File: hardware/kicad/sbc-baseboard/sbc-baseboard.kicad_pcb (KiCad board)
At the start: 4 copper layers, 140 x 80 mm, 339 parts, among them J1 USB-C upstream, J10 RJ45 magjack 10/100, J11 COM/NO/NC, J12 COM/NO/NC, J13 Console, J14 +5V_TGT out, J15 GPIO + I2C, J16 SWD, J17 Qwiic PD, J18 PSU in (isolated), J19 PSU out (isolated), J2 USB-C PD in, J3 USB-C HID to target, J4 USB-A x2, J5 USB-A x2, J601 SWD (K20), J9 FTDI header, K801 G6K-2F-Y DC5, K802 G6K-2F-Y DC5, K803 JW1FSN-DC5V, Q101 2N7002, Q102 2N7002, Q801 2N7002, Q802 2N7002, Q803 AO3400A, SW201 RESET, SW601 DAP RESET, U101 STUSB4500QTR, U102 PCA9517A, U103 TPS54560BDDA, U104 TPS54560BDDA, U105 TPS62823DLC, U201 MK64FN1M0VLL12, U202 USBLC6-2SC6, U301 KSZ8081RNA, U401 USBLC6-2SC6, U402 USB2517, U403 TPS2553DBV, U404 TPS2553DBV, U405 TPS2553DBV, U406 TPS2553DBV, U407 TPS2553DBV, U408 USBLC6-2SC6, U409 USBLC6-2SC6, U410 USBLC6-2SC6, U411 USBLC6-2SC6, U501 FT231XS, U601 MK20DX128VFM5, U701 TXB0104PW, U702 TXB0108PW, U703 TXS0102DCU, U704 TPS26630RGE, U801 LTV-817, Y201 32.768kHz, Y301 25MHz, Y401 24MHz, Y601 8MHz

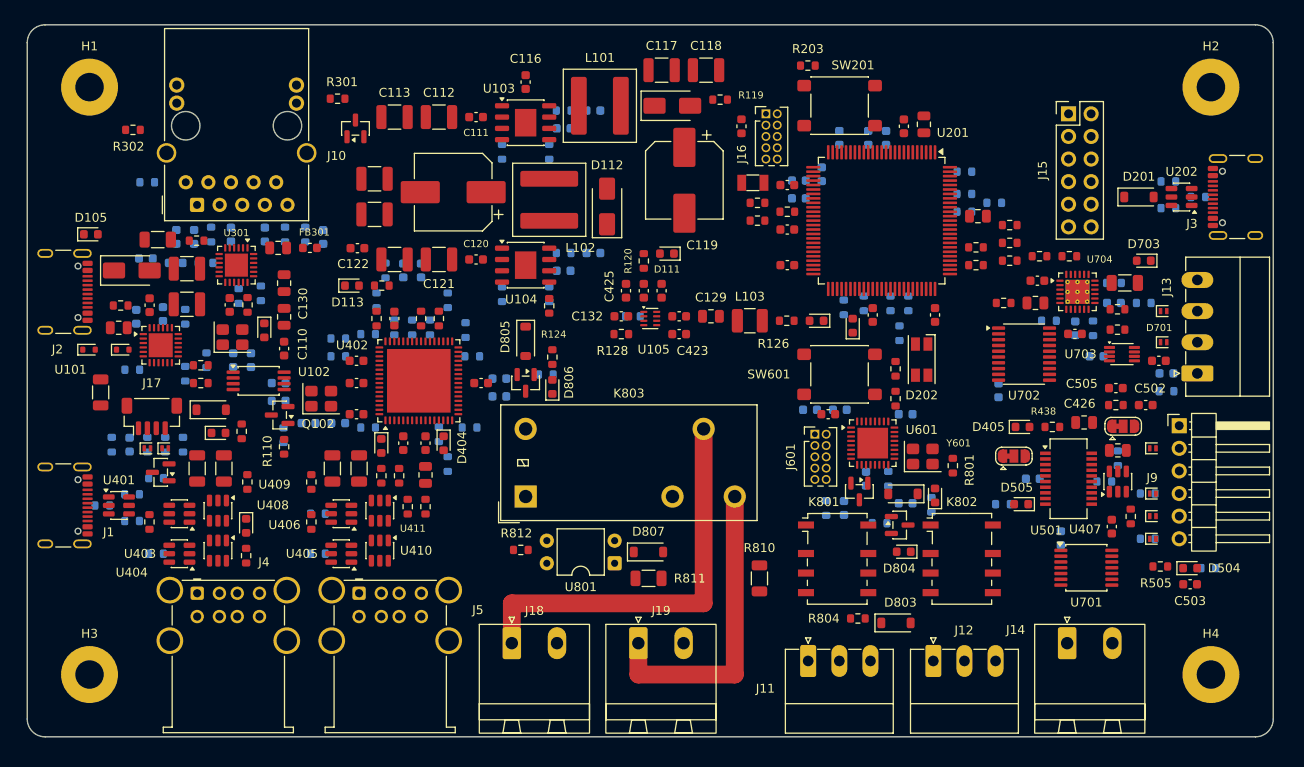
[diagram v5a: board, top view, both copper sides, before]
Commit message: Calibrate the engine against 79 published KiCad boards; the measured practice becomes the standard's numbers
scripts/reference-boards.txt and fetch-reference-boards.sh mirror Olimex,
MNT Reform, SparkFun and Raspberry Pi designs into reference-boards/
(git-ignored); scripts/harvest-placement.py measures each board with
pcbnew (decoupling distance and side, ESD and crystal distance, pad gaps,
edge clearance, bottom-side shares, tuck and through-hole margins,
designator visibility and size, track widths) into docs/reference-boards.csv;
docs/reference-boards.md records the method, the medians and the decisions.

Set from the measurement: decoupling tries its IC's first two rings on top
before the bottom (same side 77 % -> 93 %); ring gap and packing margin
0.15 mm (0.65 mm pad to pad); bottom parts tuck 1.75 mm under the IC and
keep 0.5 mm from through-hole pads; designators 0.8 mm, minimum 0.7 mm with
a 0.1 mm stroke, allowed by the board constraints (visible 61 % -> 75 %).
Kept with reason: the 3 mm edge zone. DRC unchanged, zero warnings; board
reproducible.

Co-Authored-By: Claude Fable 5.1 <noreply@anthropic.com>
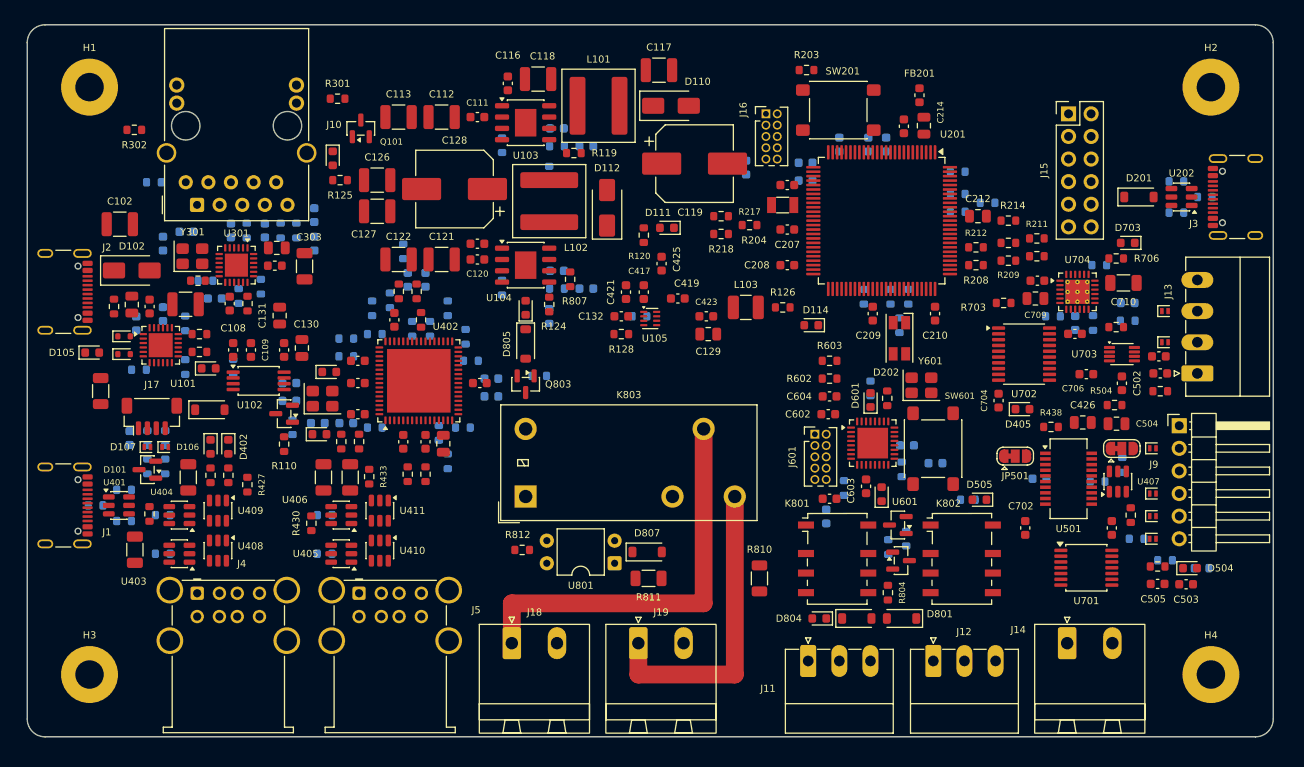
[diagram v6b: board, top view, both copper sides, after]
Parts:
- C108, C109, C602, C603, C604, C701, C702, C704, C706, R701: moved to F.Cu
- moved C505 22.5 mm to (127.0, 62.8)
- moved FB201 20.3 mm to (100.2, 7.91)
- moved C118 18.9 mm to (57.4, 6.09), turned to 180 degrees
- moved R119 17.5 mm to (61.4, 14.4)
- moved C303 16.8 mm to (31.2, 27.1), turned to -90 degrees
- moved D113 14.5 mm to (34.3, 15.0), turned to -90 degrees
- moved D801 14.0 mm to (98.2, 66.7)
- moved D404 14.0 mm to (32.8, 46.0), turned to 0 degrees
- moved C420 13.5 mm to (12.1, 59.0)
- moved C304 13.5 mm to (32.2, 24.6)
- moved C125 13.5 mm to (50.6, 24.6)
- moved SW601 13.4 mm to (101.8, 47.6), turned to 90 degrees
- moved D105 13.3 mm to (7.30, 36.8)
- moved R125 12.7 mm to (35.1, 17.4)
- moved D804 12.1 mm to (89.0, 66.7)
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
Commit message: Pairs laid as lanes, the rails as L3 regions, the Ethernet pairs named: the board ready for the bulk router
All sixteen USB 2.0 pair segments and the two Ethernet MDI pairs are laid
by the standard's placer from pair lanes in gen/layout.py: members at the
class geometry, escapes at the pads, the USB-C receptacles' doubled pads
bridged behind their rows, two pairs passing under the port pairs on the
bottom, every pair matched to within 0.25 mm, no crossings (the port
arrays and the J3 array use the house symbol drawn with I/O2 on top, the
K64's USB pins wired to its rows). J4 and J5 trade places so each stack's
pairs reach the hub row they are wired to. The ESD arrays, the series
parts and the SWD header are anchored for the lanes. The rails are
regions on In2.Cu at distinct priorities over a 3V3 base. The Ethernet
MDI pairs are named ETH_TD/RD and classed ETH (100 ohm). DRC: the 12
documented errors, no warnings but the unfilled rail islands; 499
connections for the bulk router (gen/pcb.py --route), which is running.

Co-Authored-By: Claude Fable 5.1 <noreply@anthropic.com>
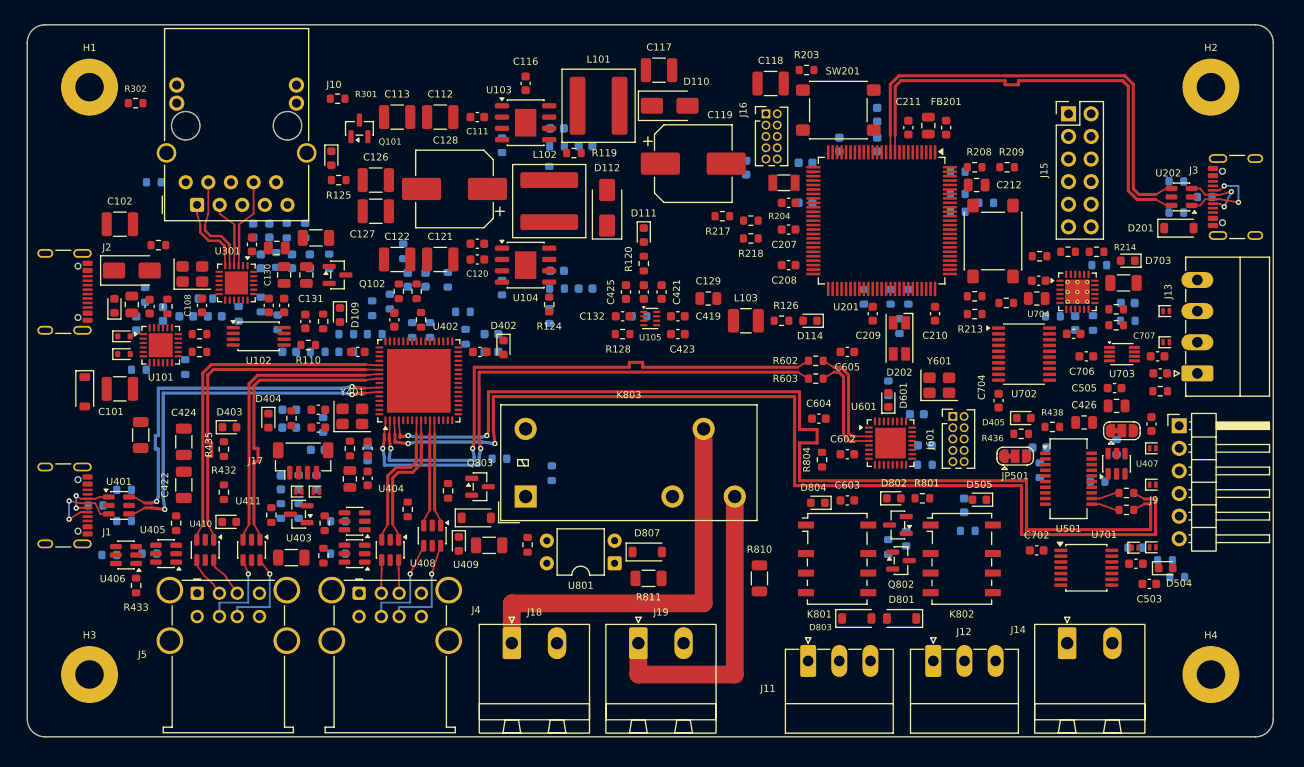
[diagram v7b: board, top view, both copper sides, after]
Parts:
- moved C420 39.8 mm to (51.9, 58.5), turned to 0 degrees
- moved R807 35.0 mm to (29.7, 44.2), turned to 90 degrees
- moved D402 32.9 mm to (53.5, 36.3)
- moved R433 28.9 mm to (12.2, 63.0), turned to 90 degrees
- moved D806 27.6 mm to (48.5, 58.3), turned to -90 degrees
- moved C118 26.1 mm to (83.5, 6.59), turned to 0 degrees
- moved R429 24.8 mm to (47.3, 52.4)
- moved R434 24.6 mm to (9.22, 59.6)
- moved U406 24.6 mm to (11.1, 59.6)
- moved SW601 24.3 mm to (108.5, 24.3)
- moved U409 24.2 mm to (45.5, 57.4)
- moved C505 22.5 mm to (122.2, 40.8)
- moved R604 22.1 mm to (113.8, 50.0)
- moved D805 20.3 mm to (50.5, 55.4), turned to 0 degrees
- moved R424 19.7 mm to (33.4, 56.0)
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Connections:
- net Net-(J10-RD+) renamed /Ethernet/ETH_RD_P
- net Net-(J10-RD-) renamed /Ethernet/ETH_RD_N
- net Net-(J10-TD+) renamed /Ethernet/ETH_TD_P
- net Net-(J10-TD-) renamed /Ethernet/ETH_TD_N
- U202 pad 1: /MCU/J3_D_N -> /MCU/J3_D_P
- U202 pad 3: /MCU/J3_D_P -> /MCU/J3_D_N
- U202 pad 4: /MCU/K64_USB_P -> /MCU/K64_USB_N
- U202 pad 6: /MCU/K64_USB_N -> /MCU/K64_USB_P
- U408 pad 1: /USB hub/HUB_DN4_N -> /USB hub/HUB_DN4_P
- U408 pad 3: /USB hub/HUB_DN4_P -> /USB hub/HUB_DN4_N
- U408 pad 4: /USB hub/PORT1_D_P -> /USB hub/PORT1_D_N
- U408 pad 6: /USB hub/PORT1_D_N -> /USB hub/PORT1_D_P
- U409 pad 1: /USB hub/HUB_DN5_N -> /USB hub/HUB_DN5_P
- U409 pad 3: /USB hub/HUB_DN5_P -> /USB hub/HUB_DN5_N
- U409 pad 4: /USB hub/PORT2_D_P -> /USB hub/PORT2_D_N
- U409 pad 6: /USB hub/PORT2_D_N -> /USB hub/PORT2_D_P
- U410 pad 1: /USB hub/HUB_DN6_N -> /USB hub/HUB_DN6_P
- U410 pad 3: /USB hub/HUB_DN6_P -> /USB hub/HUB_DN6_N
- U410 pad 4: /USB hub/PORT3_D_P -> /USB hub/PORT3_D_N
- U410 pad 6: /USB hub/PORT3_D_N -> /USB hub/PORT3_D_P
- U411 pad 1: /USB hub/HUB_DN7_N -> /USB hub/HUB_DN7_P
- U411 pad 3: /USB hub/HUB_DN7_P -> /USB hub/HUB_DN7_N
- U411 pad 4: /USB hub/PORT4_D_P -> /USB hub/PORT4_D_N
- U411 pad 6: /USB hub/PORT4_D_N -> /USB hub/PORT4_D_P
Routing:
- net HUB_DN2_P: track 0.00 -> 115.2 mm, vias 0 -> 2
- net HUB_DN2_N: track 0.00 -> 115.2 mm, vias 0 -> 2
- net HUB_DN1_N: track 0.00 -> 63.1 mm, vias 0 -> 2
- net HUB_DN1_P: track 0.00 -> 63.1 mm, vias 0 -> 2
- net /MCU/K64_USB_N: track 0.00 -> 50.9 mm
- net /MCU/K64_USB_P: track 0.00 -> 50.9 mm
- net /USB hub/HUB_UP_P: track 0.00 -> 40.7 mm, vias 0 -> 2
- net /USB hub/HUB_UP_N: track 0.00 -> 40.7 mm, vias 0 -> 2
- net /USB hub/HUB_DN6_N: track 0.00 -> 38.2 mm
- net /USB hub/HUB_DN6_P: track 0.00 -> 38.2 mm
- net /USB hub/HUB_DN7_P: track 0.00 -> 31.9 mm
- net /USB hub/HUB_DN7_N: track 0.00 -> 31.8 mm
- net /USB hub/HUB_DN4_N: track 0.00 -> 15.0 mm
- net /USB hub/HUB_DN4_P: track 0.00 -> 15.0 mm
- net /DAPLink/K20_USB_P: track 0.00 -> 12.0 mm
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- added copper zone on In2.Cu, net +3V3
- added copper zone on In2.Cu, net +5V_PORTS
- added copper zone on In2.Cu, net +5V_TGT
- added copper zone on In2.Cu, net VBUS_IN

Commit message: The board routed: the engine's lanes and pairs, then FreeRouting over them; 189 connections left for the hand pass
The autorouter ran over the locked lanes, the pair tracks and the L3
rail regions (gen/pcb.py --route: the corridors open to it, the isolation
region hardened and grown by the creepage, widths capped at 1 mm since
the planes carry the current, inner layers as planes). Twelve passes:
3067 track segments, 297 vias, 189 of 499 connections left, among them the
rail pieces still wanting vias; DRC at the 12 documented USB-C errors with
20 isolated-copper warnings for those pieces. The standards submodule is
at the tool fixes. From here the board file is the source of truth: the
hand pass finishes the connections, stitches the ground at four vias per
square centimetre and floods the outer layers.

Co-Authored-By: Claude Fable 5.1 <noreply@anthropic.com>
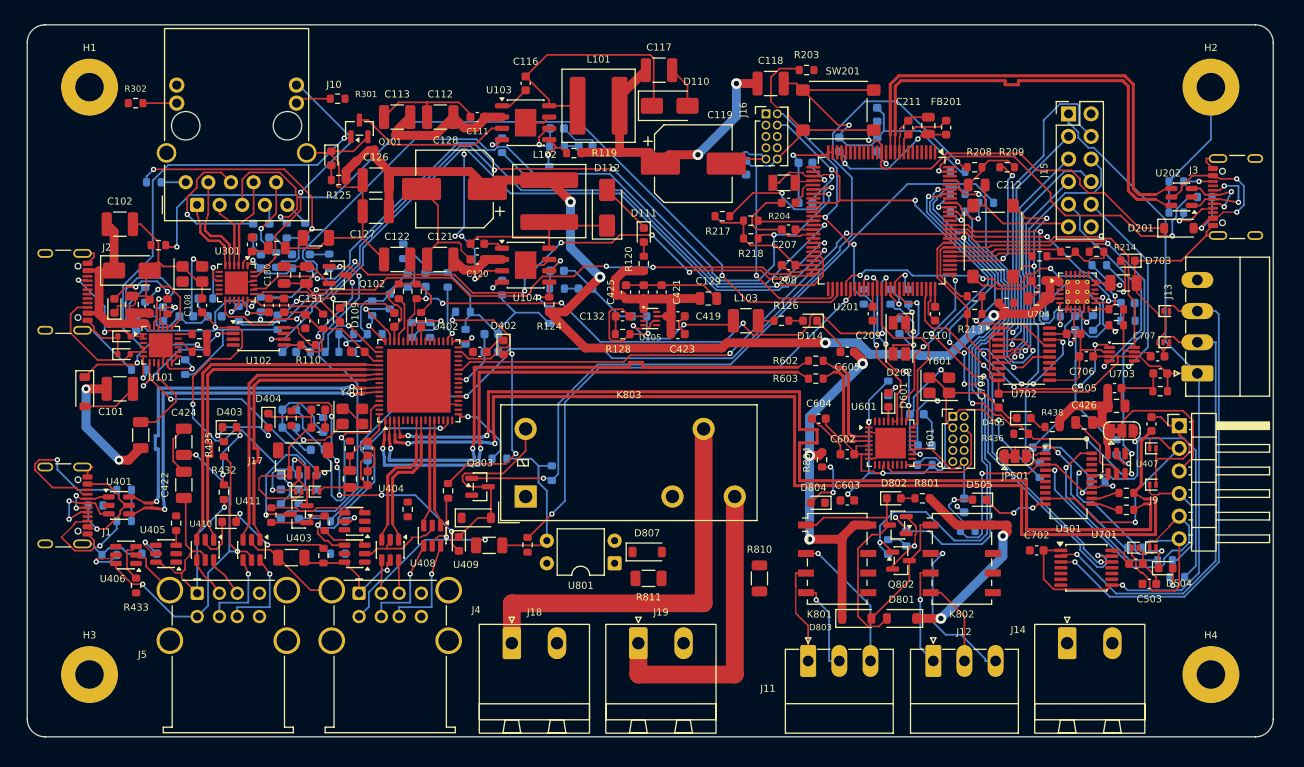
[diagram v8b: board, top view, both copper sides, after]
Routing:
- net GND: track 0.00 -> 702.0 mm, vias 0 -> 6
- net +3V3: track 0.00 -> 129.8 mm
- net +5V_PORTS: track 0.00 -> 126.8 mm, vias 0 -> 7
- net +5V_TGT: track 0.00 -> 122.0 mm, vias 0 -> 4
- net VREF_TGT: track 0.00 -> 120.7 mm, vias 0 -> 1
- net PORT1_FAULT_N: track 0.00 -> 118.1 mm, vias 0 -> 3
- net FTDI_FAULT_N: track 0.00 -> 110.7 mm, vias 0 -> 5
- net MDIO: track 0.00 -> 94.3 mm, vias 0 -> 2
- net I2C0_SDA: track 0.00 -> 91.2 mm, vias 0 -> 5
- net RMII_RXER: track 0.00 -> 88.8 mm, vias 0 -> 2
- net +3V3_PD: track 0.00 -> 87.9 mm, vias 0 -> 4
- net RMII_TXEN: track 0.00 -> 82.6 mm, vias 0 -> 2
- net RMII_RXD0: track 0.00 -> 82.5 mm, vias 0 -> 8
- net RMII_TXD0: track 0.00 -> 82.2 mm, vias 0 -> 2
- net Net-(Q803-G): track 0.00 -> 78.3 mm, vias 0 -> 1
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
